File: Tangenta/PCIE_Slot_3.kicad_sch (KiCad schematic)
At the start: 1 part, among them J4 10018784-10213TLF

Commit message: PCIe schematic continued...
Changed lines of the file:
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@@
 (kicad_sch (version 20230121) (generator eeschema)
   (paper "A4")
+  (wire (pts (xy 31.75 26.67) (xy 15.24 26.67))
+    (stroke (width 0) (type default))
+  )
+  (wire (pts (xy 31.75 38.1) (xy 15.24 38.1))
+    (stroke (width 0) (type default))
+  )
+  (wire (pts (xy 15.24 17.78) (xy 31.75 17.78))
+    (stroke (width 0) (type default))
+  )
+  (wire (pts (xy 31.75 35.56) (xy 15.24 35.56))
+    (stroke (width 0) (type default))
+  )
+  (wire (pts (xy 31.75 20.32) (xy 15.24 20.32))
+    (stroke (width 0) (type default))
+  )
+  (wire (pts (xy 31.75 24.13) (xy 15.24 24.13))
+    (stroke (width 0) (type default))
+  )
+  (wire (pts (xy 31.75 30.48) (xy 15.24 30.48))
+    (stroke (width 0) (type default))
+  )
+  (wire (pts (xy 31.75 33.02) (xy 15.24 33.02))
+    (stroke (width 0) (type default))
+  )
+  (label "PCIE3_CLK_P" (at 15.24 24.13 0) (fields_autoplaced)
+    (effects (font (size 1.27 1.27)) (justify left bottom))
+  )
+  (label "PCIE3_RX_N" (at 15.24 33.02 0) (fields_autoplaced)
+    (effects (font (size 1.27 1.27)) (justify left bottom))
+  )
+  (label "PCIE3_TX_N" (at 15.24 38.1 0) (fields_autoplaced)
+    (effects (font (size 1.27 1.27)) (justify left bottom))
+  )
+  (label "PCIE3_CLK_N" (at 15.24 26.67 0) (fields_autoplaced)
+    (effects (font (size 1.27 1.27)) (justify left bottom))
+  )
+  (label "PCIE3_TX_P" (at 15.24 35.56 0) (fields_autoplaced)
+    (effects (font (size 1.27 1.27)) (justify left bottom))
+  )
+  (label "PCIE3_PRSNT" (at 15.24 17.78 0) (fields_autoplaced)
+    (effects (font (size 1.27 1.27)) (justify left bottom))
+  )
+  (label "PCIE3_RX_P" (at 15.24 30.48 0) (fields_autoplaced)
+    (effects (font (size 1.27 1.27)) (justify left bottom))
+  )
+  (label "PCIE3_PERST" (at 15.24 20.32 0) (fields_autoplaced)
+    (effects (font (size 1.27 1.27)) (justify left bottom))
+  )
+  (hierarchical_label "PCIE3_CLK_P" (shape input) (at 31.75 24.13 0) (fields_autoplaced)
+    (effects (font (size 1.27 1.27)) (justify left))
+  )
+  (hierarchical_label "PCIE3_CLK_N" (shape input) (at 31.75 26.67 0) (fields_autoplaced)
+    (effects (font (size 1.27 1.27)) (justify left))
+  )
+  (hierarchical_label "PCIE3_TX_P" (shape input) (at 31.75 35.56 0) (fields_autoplaced)
+    (effects (font (size 1.27 1.27)) (justify left))
+  )
+  (hierarchical_label "PCIE3_PERST" (shape input) (at 31.75 20.32 0) (fields_autoplaced)
+    (effects (font (size 1.27 1.27)) (justify left))
+  )
+  (hierarchical_label "PCIE3_RX_P" (shape input) (at 31.75 30.48 0) (fields_autoplaced)
+    (effects (font (size 1.27 1.27)) (justify left))
+  )
+  (hierarchical_label "PCIE3_RX_N" (shape input) (at 31.75 33.02 0) (fields_autoplaced)
+    (effects (font (size 1.27 1.27)) (justify left))
+  )
+  (hierarchical_label "PCIE3_TX_N" (shape input) (at 31.75 38.1 0) (fields_autoplaced)
+    (effects (font (size 1.27 1.27)) (justify left))
+  )
+  (hierarchical_label "PCIE3_PRSNT" (shape input) (at 31.75 17.78 0) (fields_autoplaced)
+    (effects (font (size 1.27 1.27)) (justify left))
+  )
   (symbol (lib_id "PCIE_x16_Slot:10018784-10213TLF") (at 49.53 107.95 90) (unit 1)
     (in_bom yes) (on_board yes) (dnp no) (fields_autoplaced)

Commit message: ...
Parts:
- added R2: 0R, Resistor_SMD:R_0402_1005Metric, symbol Device:R_Small_US
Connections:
- new net PCIE3_nWAKE: R2.2
- new net nWAKE: R2.1
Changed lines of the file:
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@@
+    (stroke (width 0) (type default))
+  )
+  (wire (pts (xy 31.75 41.275) (xy 15.24 41.275))
+    (stroke (width 0) (type default))
+  )
+  (wire (pts (xy 36.83 45.72) (xy 45.72 45.72))
     (stroke (width 0) (type default))
   )
@@
     (stroke (width 0) (type default))
   )
+  (wire (pts (xy 15.24 14.605) (xy 31.75 14.605))
+    (stroke (width 0) (type default))
+  )
+  (wire (pts (xy 15.24 45.72) (xy 31.75 45.72))
+    (stroke (width 0) (type default))
+  )
   (wire (pts (xy 31.75 33.02) (xy 15.24 33.02))
     (stroke (width 0) (type default))
@@
     (effects (font (size 1.27 1.27)) (justify left bottom))
   )
+  (label "PCIE3_nWAKE" (at 15.24 41.275 0) (fields_autoplaced)
+    (effects (font (size 1.27 1.27)) (justify left bottom))
+  )
+  (label "PCIE3_nWAKE" (at 15.24 45.72 0) (fields_autoplaced)
+    (effects (font (size 1.27 1.27)) (justify left bottom))
+  )
   (label "PCIE3_TX_N" (at 15.24 38.1 0) (fields_autoplaced)
     (effects (font (size 1.27 1.27)) (justify left bottom))
@@
     (effects (font (size 1.27 1.27)) (justify left bottom))
   )
+  (label "12V" (at 15.24 14.605 0) (fields_autoplaced)
+    (effects (font (size 1.27 1.27)) (justify left bottom))
+  )
   (label "PCIE3_TX_P" (at 15.24 35.56 0) (fields_autoplaced)
     (effects (font (size 1.27 1.27)) (justify left bottom))
   )
+  (label "nWAKE" (at 45.72 45.72 180) (fields_autoplaced)
+    (effects (font (size 1.27 1.27)) (justify right bottom))
+  )
   (label "PCIE3_PRSNT" (at 15.24 17.78 0) (fields_autoplaced)
     (effects (font (size 1.27 1.27)) (justify left bottom))
@@
     (effects (font (size 1.27 1.27)) (justify left bottom))
   )
+  (hierarchical_label "12V" (shape input) (at 31.75 14.605 0) (fields_autoplaced)
+    (effects (font (size 1.27 1.27)) (justify left))
+  )
   (hierarchical_label "PCIE3_CLK_P" (shape input) (at 31.75 24.13 0) (fields_autoplaced)
     (effects (font (size 1.27 1.27)) (justify left))
@@
   )
   (hierarchical_label "PCIE3_RX_N" (shape input) (at 31.75 33.02 0) (fields_autoplaced)
+    (effects (font (size 1.27 1.27)) (justify left))
+  )
+  (hierarchical_label "PCIE3_nWAKE" (shape input) (at 31.75 41.275 0) (fields_autoplaced)
     (effects (font (size 1.27 1.27)) (justify left))
   )
@@
         )
       )
+    )
+  )
+  (symbol (lib_id "Device:R_Small_US") (at 34.29 45.72 270) (unit 1)
+    (in_bom yes) (on_board yes) (dnp no)
+    (property "Reference" "R2" (at 28.575 44.45 90)
+      (effects (font (size 1.27 1.27)) (justify left))
+    )
+    (property "Value" "0R" (at 35.56 44.45 90)
+      (effects (font (size 1.27 1.27)) (justify left))
+    )
+    (property "Footprint" "Resistor_SMD:R_0402_1005Metric" (at 34.29 45.72 0)
+      (effects (font (size 1.27 1.27)) hide)
+    )
+    (property "Datasheet" "~" (at 34.29 45.72 0)
+      (effects (font (size 1.27 1.27)) hide)
+    )
+    (pin "1")
+    (pin "2")
+    (instances
+      (project "Tangenta"
+        (path "/358d1bcf-7599-4352-8c4d-baa18a5f09e6/8215796b-9611-4f43-bcc5-319f8414b8a6"
+          (reference "R2") (unit 1)
+        )
+        (path "/358d1bcf-7599-4352-8c4d-baa18a5f09e6/d6c05402-162e-441f-bed8-be7996260fb4"
+          (reference "R18") (unit 1)
+        )
+        (path "/358d1bcf-7599-4352-8c4d-baa18a5f09e6/b1871a4d-6a35-44e2-a9a2-9a4af684371d"
+          (reference "R26") (unit 1)
+        )
+        (path "/358d1bcf-7599-4352-8c4d-baa18a5f09e6/6a8c68b5-4a7d-449e-86f6-34ced6d1cb55"
+          (reference "R41") (unit 1)
+        )
+        (path "/358d1bcf-7599-4352-8c4d-baa18a5f09e6/db297b0b-35f2-4e86-892c-83973f1ac2db"
+          (reference "R56") (unit 1)
+        )
+        (path "/358d1bcf-7599-4352-8c4d-baa18a5f09e6/9b1f6f94-444c-4c59-8de9-290bde336856/79105fff-2111-4675-95ec-60397c562e45"
+          (reference "R62") (unit 1)
+        )
+        (path "/358d1bcf-7599-4352-8c4d-baa18a5f09e6/9b1f6f94-444c-4c59-8de9-290bde336856/95d5fed9-c617-43f1-96e2-65308e862f66"
+          (reference "R64") (unit 1)
+        )
+      )

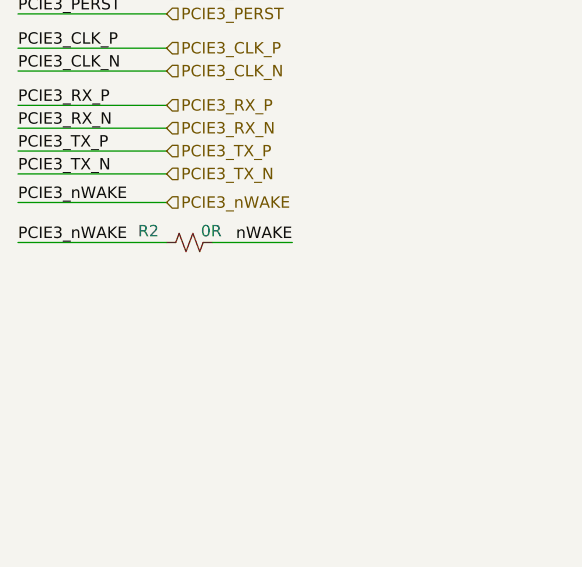
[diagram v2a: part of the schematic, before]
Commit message: PCIe switch schematic, continued...
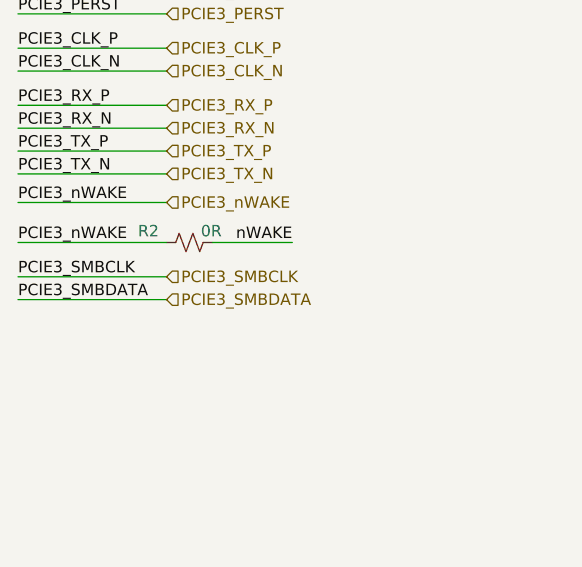
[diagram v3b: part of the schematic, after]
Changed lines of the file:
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@@
+    (stroke (width 0) (type default))
+  )
+  (wire (pts (xy 31.75 52.07) (xy 15.24 52.07))
     (stroke (width 0) (type default))
   )
@@
     (stroke (width 0) (type default))
   )
+  (wire (pts (xy 31.75 49.53) (xy 15.24 49.53))
+    (stroke (width 0) (type default))
+  )
   (label "PCIE3_CLK_P" (at 15.24 24.13 0) (fields_autoplaced)
     (effects (font (size 1.27 1.27)) (justify left bottom))
@@
     (effects (font (size 1.27 1.27)) (justify left bottom))
   )
+  (label "PCIE3_SMBDATA" (at 15.24 52.07 0) (fields_autoplaced)
+    (effects (font (size 1.27 1.27)) (justify left bottom))
+  )
   (label "PCIE3_TX_N" (at 15.24 38.1 0) (fields_autoplaced)
     (effects (font (size 1.27 1.27)) (justify left bottom))
   )
   (label "PCIE3_CLK_N" (at 15.24 26.67 0) (fields_autoplaced)
+    (effects (font (size 1.27 1.27)) (justify left bottom))
+  )
+  (label "PCIE3_SMBCLK" (at 15.24 49.53 0) (fields_autoplaced)
     (effects (font (size 1.27 1.27)) (justify left bottom))
   )
@@
     (effects (font (size 1.27 1.27)) (justify left))
   )
+  (hierarchical_label "PCIE3_SMBDATA" (shape input) (at 31.75 52.07 0) (fields_autoplaced)
+    (effects (font (size 1.27 1.27)) (justify left))
+  )
+  (hierarchical_label "PCIE3_SMBCLK" (shape input) (at 31.75 49.53 0) (fields_autoplaced)
+    (effects (font (size 1.27 1.27)) (justify left))
+  )

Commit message: ...
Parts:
- added C23 (x2): 47uF, CAP_L6:CAP_L6, symbol CAP_L6:35CE47AX
- added C24 (x2): 47uF, CAP_TANTAL_A:CAP_TANTAL_A, symbol CAP_TANTAL_A:CA45-A-6_3V-47UF-K
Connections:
- net 12V: now also C23.1, C23.1
- new net 3V3: C24.1, C24.1
- new net GND: C23.2, C23.2, C24.2, C24.2
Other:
- moved on the sheet: J4

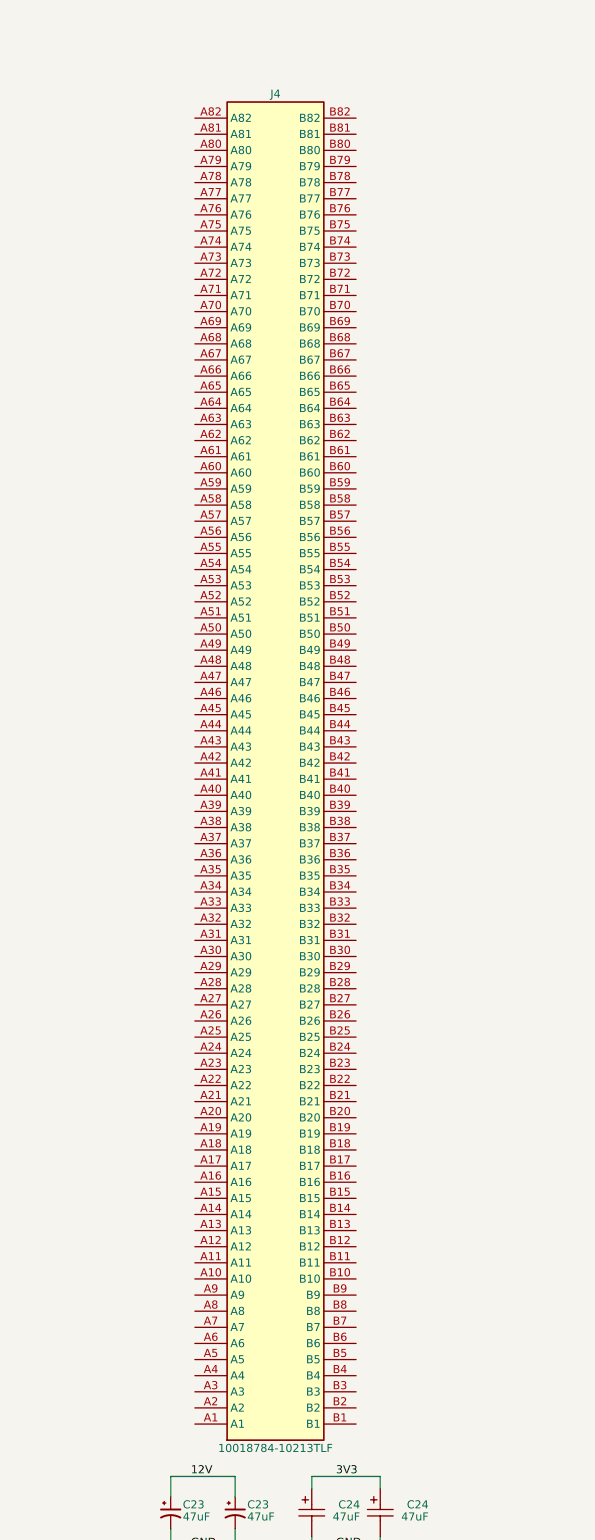
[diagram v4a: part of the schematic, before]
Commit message: PCIe position revisited.
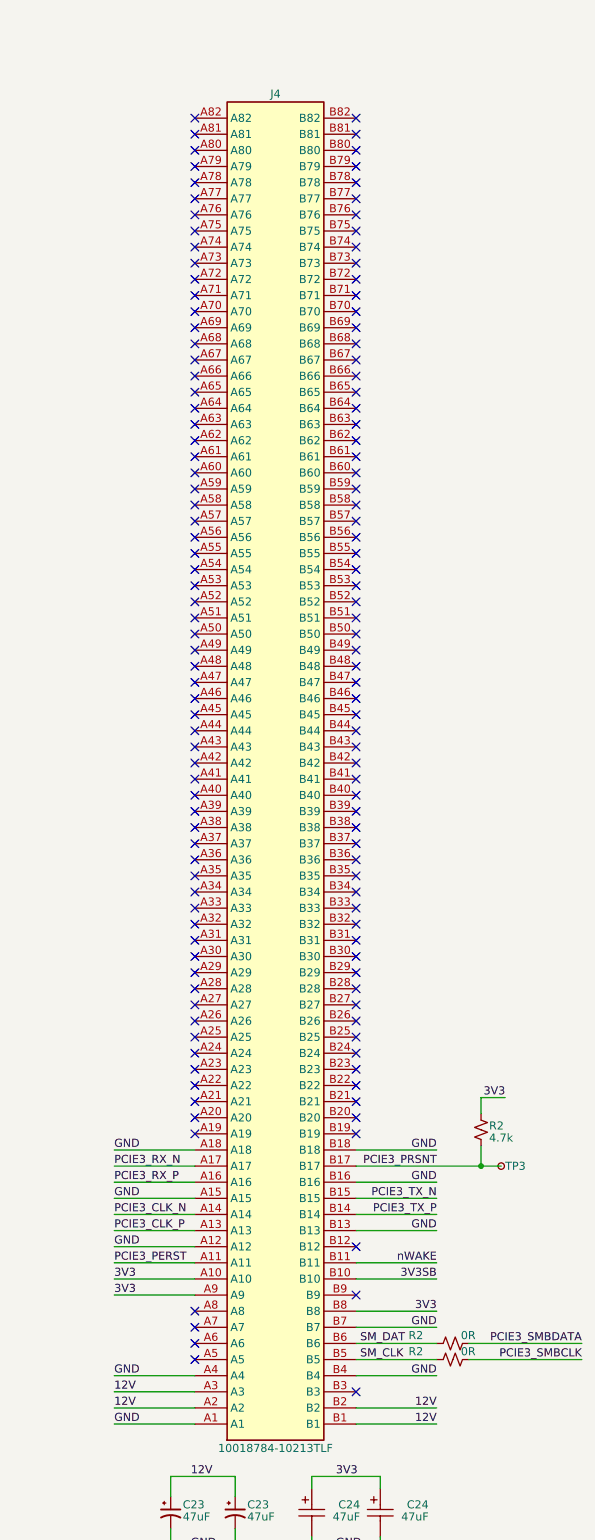
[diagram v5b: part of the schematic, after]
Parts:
- added R2 (x2): 0R, Resistor_SMD:R_0402_1005Metric, symbol Device:R_Small_US
- added R2: 4.7k, Resistor_SMD:R_0402_1005Metric, symbol Device:R_Small_US
- added TP3: TestPoint_Small, TestPoint:TestPoint_Pad_1.0x1.0mm, symbol Connector:TestPoint_Small
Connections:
- net 12V: now also J4.A2, J4.A3, J4.B1, J4.B2
- net 3V3: now also J4.A10, J4.A9, J4.B8, R2.1
- net 3V3_STANDBY: now also J4.B10
- net GND: now also J4.A1, J4.A12, J4.A15, J4.A18, J4.A4, J4.B13, J4.B16, J4.B18, J4.B4, J4.B7
- net PCIE3_CLK_N: now also J4.A14
- net PCIE3_CLK_P: now also J4.A13
- net PCIE3_PERST: now also J4.A11
- net PCIE3_PRSNT: now also J4.B17, R2.2, TP3.1
- net PCIE3_RX_N: now also J4.A17
- net PCIE3_RX_P: now also J4.A16
- net PCIE3_SMBCLK: now also R2.1
- net PCIE3_SMBDATA: now also R2.1
- net PCIE3_TX_N: now also J4.B15
- net PCIE3_TX_P: now also J4.B14
- net nWAKE: now also J4.B11
- net SM_CLK: now reaches J4.B5
- net SM_CLK: now also R2.2
- net SM_DAT: now reaches J4.B6
- net SM_DAT: now also R2.2
- no-connect marks 0 -> 135

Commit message: Libraries exported from global to project.
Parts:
- C23: symbol CAP_L6:35CE47AX -> CholaSymbolsPrjLib:35CE47AX
- C24: symbol CAP_TANTAL_A:CA45-A-6_3V-47UF-K -> CholaSymbolsPrjLib:CA45-A-6_3V-47UF-K
- J4: symbol PCIE_x16_Slot:10018784-10213TLF -> CholaSymbolsPrjLib:10018784-10213TLF
- R2: symbol Device:R_Small_US -> CholaSymbolsPrjLib:R_Small_US
- TP3: symbol Connector:TestPoint_Small -> CholaSymbolsPrjLib:TestPoint_Small
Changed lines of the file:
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@@
     (effects (font (size 1.27 1.27)) (justify left))
   )
-  (symbol (lib_id "Device:R_Small_US") (at 237.49 236.855 270) (unit 1)
+  (symbol (lib_id "CholaSymbolsPrjLib:R_Small_US") (at 237.49 236.855 270) (unit 1)
     (in_bom yes) (on_board yes) (dnp no)
     (property "Reference" "R2" (at 230.505 235.585 90)
@@
     )
   )
-  (symbol (lib_id "Device:R_Small_US") (at 237.49 239.395 270) (unit 1)
+  (symbol (lib_id "CholaSymbolsPrjLib:R_Small_US") (at 237.49 239.395 270) (unit 1)
     (in_bom yes) (on_board yes) (dnp no)
     (property "Reference" "R2" (at 230.505 238.125 90)
@@
     )
   )
-  (symbol (lib_id "CAP_TANTAL_A:CA45-A-6_3V-47UF-K") (at 215.265 263.525 270) (mirror x) (unit 1)
+  (symbol (lib_id "CholaSymbolsPrjLib:CA45-A-6_3V-47UF-K") (at 215.265 263.525 270) (mirror x) (unit 1)
     (in_bom yes) (on_board yes) (dnp no)
     (property "Reference" "C24" (at 222.885 262.255 90)
@@
     )
   )
-  (symbol (lib_id "PCIE_x16_Slot:10018784-10213TLF") (at 196.85 249.555 0) (mirror x) (unit 1)
+  (symbol (lib_id "CholaSymbolsPrjLib:10018784-10213TLF") (at 196.85 249.555 0) (mirror x) (unit 1)
     (in_bom yes) (on_board yes) (dnp no)
     (property "Reference" "J4" (at 209.55 40.005 0)
@@
     )
   )
-  (symbol (lib_id "Device:R_Small_US") (at 34.29 45.72 270) (unit 1)
+  (symbol (lib_id "CholaSymbolsPrjLib:R_Small_US") (at 34.29 45.72 270) (unit 1)
     (in_bom yes) (on_board yes) (dnp no)
     (property "Reference" "R2" (at 28.575 44.45 90)
@@
     )
   )
-  (symbol (lib_id "Device:R_Small_US") (at 241.935 203.2 0) (unit 1)
+  (symbol (lib_id "CholaSymbolsPrjLib:R_Small_US") (at 241.935 203.2 0) (unit 1)
     (in_bom yes) (on_board yes) (dnp no)
     (property "Reference" "R2" (at 243.205 202.565 0)
@@
     )
   )
-  (symbol (lib_id "CAP_L6:35CE47AX") (at 203.2 263.525 0) (unit 1)
+  (symbol (lib_id "CholaSymbolsPrjLib:35CE47AX") (at 203.2 263.525 0) (unit 1)
     (in_bom yes) (on_board yes) (dnp no)
     (property "Reference" "C23" (at 205.105 262.255 0)
@@
     )
   )
-  (symbol (lib_id "CAP_TANTAL_A:CA45-A-6_3V-47UF-K") (at 226.06 263.525 270) (mirror x) (unit 1)
+  (symbol (lib_id "CholaSymbolsPrjLib:CA45-A-6_3V-47UF-K") (at 226.06 263.525 270) (mirror x) (unit 1)
     (in_bom yes) (on_board yes) (dnp no)
     (property "Reference" "C24" (at 233.68 262.255 90)
@@
     )
   )
-  (symbol (lib_id "Connector:TestPoint_Small") (at 245.11 208.915 0) (unit 1)
+  (symbol (lib_id "CholaSymbolsPrjLib:TestPoint_Small") (at 245.11 208.915 0) (unit 1)
     (in_bom yes) (on_board yes) (dnp no)
     (property "Reference" "TP3" (at 245.745 208.915 0)
@@
     )
   )
-  (symbol (lib_id "CAP_L6:35CE47AX") (at 193.04 263.525 0) (unit 1)
+  (symbol (lib_id "CholaSymbolsPrjLib:35CE47AX") (at 193.04 263.525 0) (unit 1)
     (in_bom yes) (on_board yes) (dnp no)
     (property "Reference" "C23" (at 194.945 262.255 0)

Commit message: initialize branch
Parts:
- renumbered C23 to C114, C23 to C115, C24 to C116, C24 to C117, J4 to J20, R2 to R88, R2 to R89, R2 to R90, R2 to R91
